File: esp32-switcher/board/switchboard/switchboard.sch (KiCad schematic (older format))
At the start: 15 parts, among them J1 Conn_01x03, J10 Conn_01x02, J11 Conn_01x02, J12 Conn_01x02, J13 Conn_01x02, J14 Conn_01x02, J2 Conn_01x04, J3 Conn_01x02, J4 Conn_01x02, J5 Conn_01x02, J6 Conn_01x02, J7 Conn_01x02, J8 Conn_01x02, J9 Conn_01x02, U1 ESP32-DEVKITC-32D

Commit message: Updates, almost ready to go
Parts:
- added J15: Chain Out, Connector_JST:JST_XH_B3B-XH-AM_1x03_P2.50mm_Vertical, symbol Connector_Generic:Conn_01x03
- J16: renamed from J1; value Conn_01x03 -> Chain In
- U1: value ESP32-DEVKITC-32D -> NODEMCU-32S
- renumbered J3 to J1, J9 to J11, J8 to J12, J2 to J17, J4 to J2, J5 to J3, J6 to J4, J7 to J5, J14 to J6, J13 to J7, J12 to J8, J11 to J9
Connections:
- net GND: now also J15.2 (Pin_2)
- net at J16.1 (Pin_1), U1.29 (IO5): now also J15.1 (Pin_1)
- net at J16.3 (Pin_3), U1.32 (IO4): now also J15.3 (Pin_3)
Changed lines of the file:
@@
 EESchema Schematic File Version 4
+LIBS:switchboard-cache
 EELAYER 29 0
 EELAYER END
@@
 $EndDescr
 $Comp
-L Connector_Generic:Conn_01x03 J1
+L Connector_Generic:Conn_01x03 J16
 U 1 1 5CA18F92
 P 6900 5150
-F 0 "J1" V 6772 5330 50  0000 L CNN
-F 1 "Conn_01x03" V 6863 5330 50  0000 L CNN
+F 0 "J16" V 6772 5330 50  0000 L CNN
+F 1 "Chain In" V 6863 5330 50  0000 L CNN
 F 2 "Connector_JST:JST_XH_B3B-XH-AM_1x03_P2.50mm_Vertical" H 6900 5150 50  0001 C CNN
 F 3 "~" H 6900 5150 50  0001 C CNN
@@
 $EndComp
 $Comp
-L Connector_Generic:Conn_01x02 J3
+L Connector_Generic:Conn_01x02 J1
 U 1 1 5CA196A9
 P 7950 2900
-F 0 "J3" H 8030 2892 50  0000 L CNN
+F 0 "J1" H 8030 2892 50  0000 L CNN
 F 1 "Conn_01x02" H 8030 2801 50  0000 L CNN
 F 2 "Connector_JST:JST_XH_B2B-XH-AM_1x02_P2.50mm_Vertical" H 7950 2900 50  0001 C CNN
@@
 $EndComp
 $Comp
-L Connector_Generic:Conn_01x04 J2
+L Connector_Generic:Conn_01x04 J17
 U 1 1 5CA19C8A
 P 6600 2250
-F 0 "J2" V 6564 1962 50  0000 R CNN
+F 0 "J17" V 6564 1962 50  0000 R CNN
 F 1 "Conn_01x04" V 6473 1962 50  0000 R CNN
 F 2 "Connector_PinSocket_2.54mm:PinSocket_1x04_P2.54mm_Vertical" H 6600 2250 50  0001 C CNN
@@
 $EndComp
 $Comp
-L Connector_Generic:Conn_01x02 J4
+L Connector_Generic:Conn_01x02 J2
 U 1 1 5CA1C04C
 P 7950 3150
-F 0 "J4" H 8030 3142 50  0000 L CNN
+F 0 "J2" H 8030 3142 50  0000 L CNN
 F 1 "Conn_01x02" H 8030 3051 50  0000 L CNN
 F 2 "Connector_JST:JST_XH_B2B-XH-AM_1x02_P2.50mm_Vertical" H 7950 3150 50  0001 C CNN
@@
 $EndComp
 $Comp
-L Connector_Generic:Conn_01x02 J5
+L Connector_Generic:Conn_01x02 J3
 U 1 1 5CA1C459
 P 7950 3400
-F 0 "J5" H 8030 3392 50  0000 L CNN
+F 0 "J3" H 8030 3392 50  0000 L CNN
 F 1 "Conn_01x02" H 8030 3301 50  0000 L CNN
 F 2 "Connector_JST:JST_XH_B2B-XH-AM_1x02_P2.50mm_Vertical" H 7950 3400 50  0001 C CNN
@@
 $EndComp
 $Comp
-L Connector_Generic:Conn_01x02 J6
+L Connector_Generic:Conn_01x02 J4
 U 1 1 5CA1E338
 P 7950 3650
-F 0 "J6" H 8030 3642 50  0000 L CNN
+F 0 "J4" H 8030 3642 50  0000 L CNN
 F 1 "Conn_01x02" H 8030 3551 50  0000 L CNN
 F 2 "Connector_JST:JST_XH_B2B-XH-AM_1x02_P2.50mm_Vertical" H 7950 3650 50  0001 C CNN
@@
 $EndComp
 $Comp
-L Connector_Generic:Conn_01x02 J7
+L Connector_Generic:Conn_01x02 J5
 U 1 1 5CA1E6C2
 P 7950 3900
-F 0 "J7" H 8030 3892 50  0000 L CNN
+F 0 "J5" H 8030 3892 50  0000 L CNN
 F 1 "Conn_01x02" H 8030 3801 50  0000 L CNN
 F 2 "Connector_JST:JST_XH_B2B-XH-AM_1x02_P2.50mm_Vertical" H 7950 3900 50  0001 C CNN
@@
 $EndComp
 $Comp
-L Connector_Generic:Conn_01x02 J8
+L Connector_Generic:Conn_01x02 J12
 U 1 1 5CA1E911
 P 3450 4500
-F 0 "J8" H 3530 4492 50  0000 L CNN
+F 0 "J12" H 3530 4492 50  0000 L CNN
 F 1 "Conn_01x02" H 3530 4401 50  0000 L CNN
 F 2 "Connector_JST:JST_XH_B2B-XH-AM_1x02_P2.50mm_Vertical" H 3450 4500 50  0001 C CNN
@@
 $EndComp
 $Comp
-L Connector_Generic:Conn_01x02 J9
+L Connector_Generic:Conn_01x02 J11
 U 1 1 5CA1EDBC
 P 3450 4250
-F 0 "J9" H 3530 4242 50  0000 L CNN
+F 0 "J11" H 3530 4242 50  0000 L CNN
 F 1 "Conn_01x02" H 3530 4151 50  0000 L CNN
 F 2 "Connector_JST:JST_XH_B2B-XH-AM_1x02_P2.50mm_Vertical" H 3450 4250 50  0001 C CNN
@@
 $EndComp
 $Comp
-L Connector_Generic:Conn_01x02 J11
+L Connector_Generic:Conn_01x02 J9
 U 1 1 5CA1F5C5
 P 3450 3750
-F 0 "J11" H 3530 3742 50  0000 L CNN
+F 0 "J9" H 3530 3742 50  0000 L CNN
 F 1 "Conn_01x02" H 3530 3651 50  0000 L CNN
 F 2 "Connector_JST:JST_XH_B2B-XH-AM_1x02_P2.50mm_Vertical" H 3450 3750 50  0001 C CNN
@@
 $EndComp
 $Comp
-L Connector_Generic:Conn_01x02 J12
+L Connector_Generic:Conn_01x02 J8
 U 1 1 5CA1F98B
 P 3450 3500
-F 0 "J12" H 3530 3492 50  0000 L CNN
+F 0 "J8" H 3530 3492 50  0000 L CNN
 F 1 "Conn_01x02" H 3530 3401 50  0000 L CNN
 F 2 "Connector_JST:JST_XH_B2B-XH-AM_1x02_P2.50mm_Vertical" H 3450 3500 50  0001 C CNN
@@
 $EndComp
 $Comp
-L Connector_Generic:Conn_01x02 J13
+L Connector_Generic:Conn_01x02 J7
 U 1 1 5CA1FBF3
 P 3450 3250
-F 0 "J13" H 3530 3242 50  0000 L CNN
+F 0 "J7" H 3530 3242 50  0000 L CNN
 F 1 "Conn_01x02" H 3530 3151 50  0000 L CNN
 F 2 "Connector_JST:JST_XH_B2B-XH-AM_1x02_P2.50mm_Vertical" H 3450 3250 50  0001 C CNN
@@
 $EndComp
 $Comp
-L Connector_Generic:Conn_01x02 J14
+L Connector_Generic:Conn_01x02 J6
 U 1 1 5CA1FEDD
 P 3450 3000
-F 0 "J14" H 3530 2992 50  0000 L CNN
+F 0 "J6" H 3530 2992 50  0000 L CNN
 F 1 "Conn_01x02" H 3530 2901 50  0000 L CNN
 F 2 "Connector_JST:JST_XH_B2B-XH-AM_1x02_P2.50mm_Vertical" H 3450 3000 50  0001 C CNN
@@
 P 5500 3700
 F 0 "U1" H 5500 4867 50  0000 C CNN
-F 1 "ESP32-DEVKITC-32D" H 5500 4776 50  0000 C CNN
+F 1 "NODEMCU-32S" H 5500 4776 50  0000 C CNN
 F 2 "MODULE_ESP32-DEVKITC-32D" H 5500 3700 50  0001 L BNN
 F 3 "" H 5500 3700 50  0001 L BNN
@@
 	6300 3600 7100 3600
 Wire Wire Line
-	6800 4000 6800 4950
-Wire Wire Line
-	7000 3700 7000 4950
+	6800 4000 6800 4550
+Wire Wire Line
+	7000 3700 7000 4650
 Text GLabel 6900 4950 1    50   Input ~ 0
 GND
@@
 Wire Wire Line
 	4350 4500 3650 4500
+$Comp
+L Connector_Generic:Conn_01x03 J15
+U 1 1 5CA1AEFD
+P 7800 5150
+F 0 "J15" V 7672 5330 50  0000 L CNN
+F 1 "Chain Out" V 7763 5330 50  0000 L CNN
+F 2 "Connector_JST:JST_XH_B3B-XH-AM_1x03_P2.50mm_Vertical" H 7800 5150 50  0001 C CNN
+F 3 "~" H 7800 5150 50  0001 C CNN
+	1    7800 5150
+	0    1    1    0
+$EndComp
+Text GLabel 7800 4950 1    50   Input ~ 0
+GND
+Wire Wire Line
+	6800 4550 7700 4550
+Wire Wire Line
+	7700 4550 7700 4950
+Connection ~ 6800 4550
+Wire Wire Line
+	6800 4550 6800 4950
+Wire Wire Line
+	7000 4650 7900 4650
+Wire Wire Line
+	7900 4650 7900 4950
+Connection ~ 7000 4650
+Wire Wire Line
+	7000 4650 7000 4950
 $EndSCHEMATC

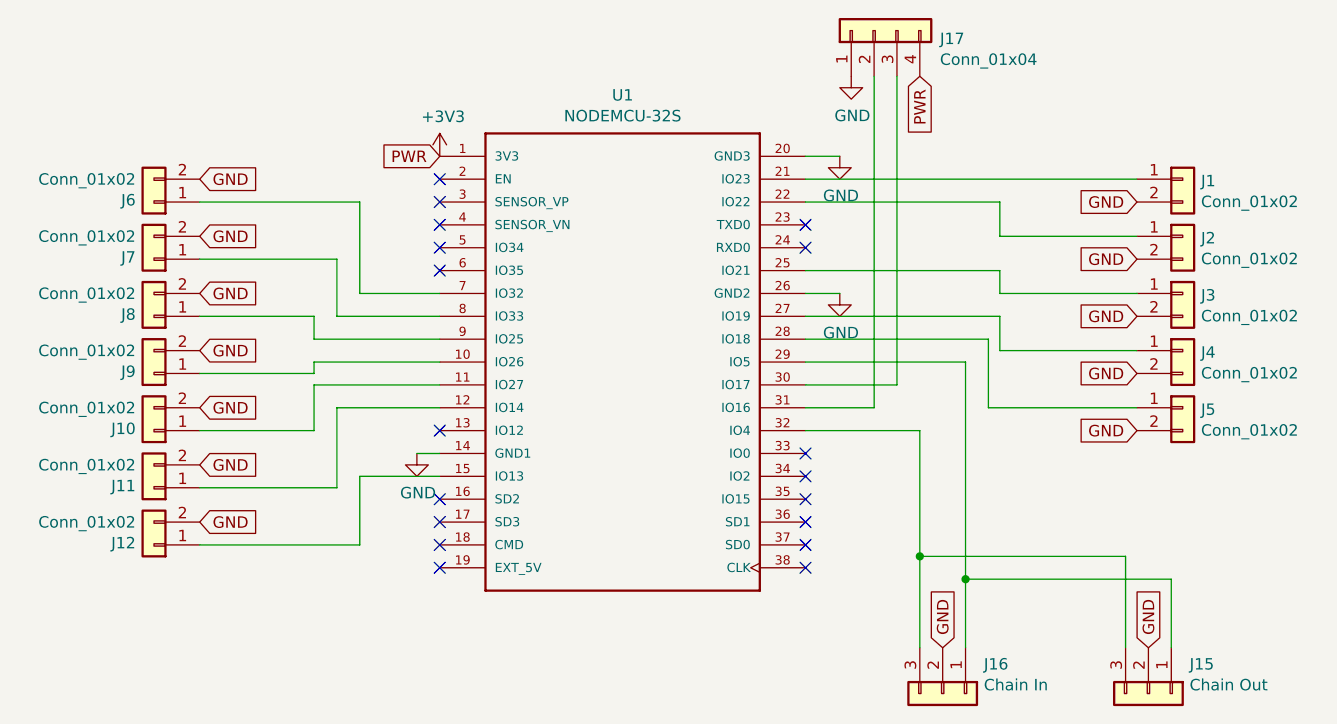
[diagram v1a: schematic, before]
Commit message: Rev 1.1 of ESP32 Switchboard
I think this rev is basically ready to go. I could see someone using
this for real. I still have a lot of software features I wanna add, but
the hardware is basically complete.

I may come back and add a built-in serial port, as the little breakout
can be flimsy, but it seems that 3v3 rs232 stuff means SMD components,
and I've been trying to avoid that to make this easier to DIY.

board:
  Converted footprint to Kicad non-legacy
  Fixed footprint to be HiLetGo ESP-E32, which is narrower than NodeMCU
  Fixed up references on schematic to be in order
  Flipped mistaken footprint on RS232 UART breakout

code:
  Added support for all 12 inputs
  IRQ-based on rising/falling edges
  Added 0.1s timer-based timeout for input switch after input off
    Fixes some bouncing in the signal I didn't expect when powering off
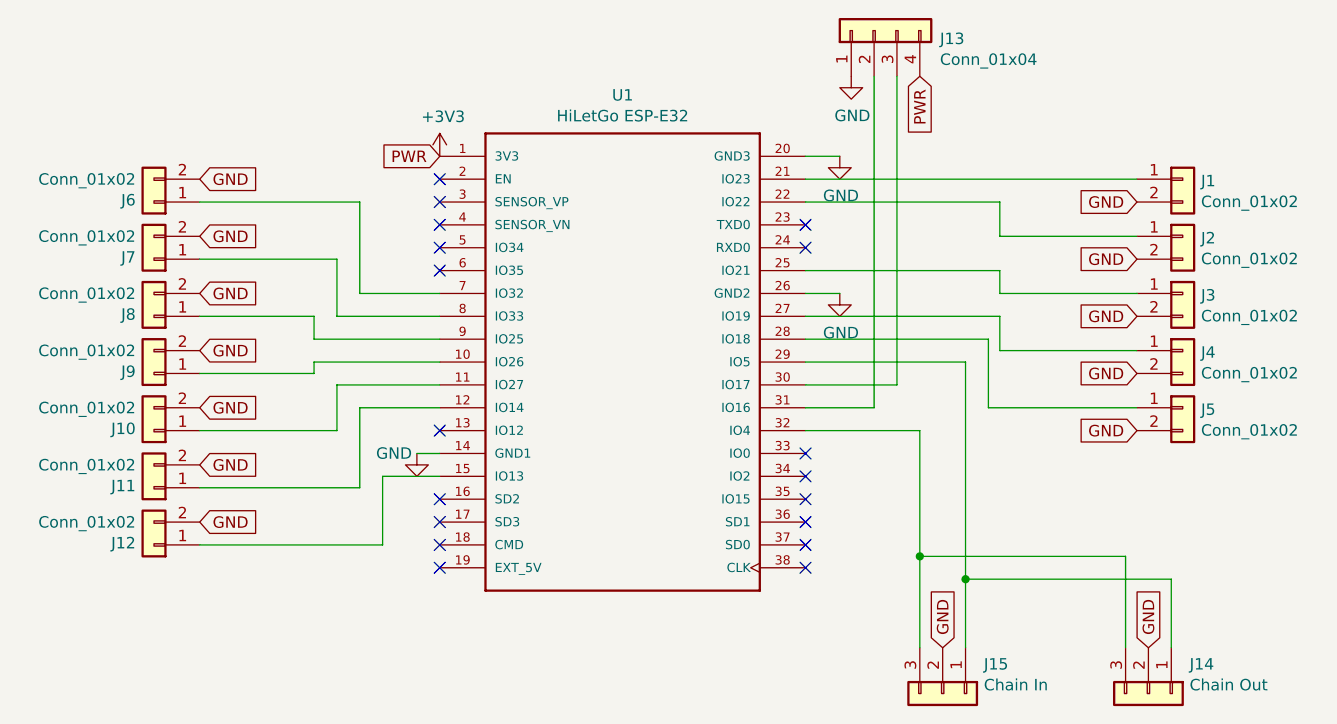
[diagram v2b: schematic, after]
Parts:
- U1: value NODEMCU-32S -> HiLetGo ESP-E32; footprint MODULE_ESP32-DEVKITC-32D -> hiletgo-e32:HILETGO-E32
- renumbered J17 to J13, J15 to J14, J16 to J15
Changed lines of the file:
@@
 encoding utf-8
 Sheet 1 1
-Title ""
-Date ""
-Rev ""
-Comp ""
-Comment1 ""
+Title "Extron ESP32 Switchboard"
+Date "2019-04-05"
+Rev "1.1"
+Comp "Rattboi (Bradon Kanyid)"
+Comment1 "https://github.com/rattboi/extron-scart-adapter"
 Comment2 ""
 Comment3 ""
@@
 $EndDescr
 $Comp
-L Connector_Generic:Conn_01x03 J16
+L Connector_Generic:Conn_01x03 J15
 U 1 1 5CA18F92
 P 6900 5150
-F 0 "J16" V 6772 5330 50  0000 L CNN
+F 0 "J15" V 6772 5330 50  0000 L CNN
 F 1 "Chain In" V 6863 5330 50  0000 L CNN
 F 2 "Connector_JST:JST_XH_B3B-XH-AM_1x03_P2.50mm_Vertical" H 6900 5150 50  0001 C CNN
@@
 $EndComp
 $Comp
-L Connector_Generic:Conn_01x04 J17
+L Connector_Generic:Conn_01x04 J13
 U 1 1 5CA19C8A
 P 6600 2250
-F 0 "J17" V 6564 1962 50  0000 R CNN
+F 0 "J13" V 6564 1962 50  0000 R CNN
 F 1 "Conn_01x04" V 6473 1962 50  0000 R CNN
 F 2 "Connector_PinSocket_2.54mm:PinSocket_1x04_P2.54mm_Vertical" H 6600 2250 50  0001 C CNN
@@
 P 4600 4100
 F 0 "#PWR0105" H 4600 3850 50  0001 C CNN
-F 1 "GND" H 4605 3927 50  0000 C CNN
+F 1 "GND" H 4500 4100 50  0000 C CNN
 F 2 "" H 4600 4100 50  0001 C CNN
 F 3 "" H 4600 4100 50  0001 C CNN
@@
 NoConn ~ 6300 4300
 Wire Wire Line
-	4700 4200 4350 4200
-Wire Wire Line
 	6300 3000 7150 3000
 Wire Wire Line
@@
 P 5500 3700
 F 0 "U1" H 5500 4867 50  0000 C CNN
-F 1 "NODEMCU-32S" H 5500 4776 50  0000 C CNN
-F 2 "MODULE_ESP32-DEVKITC-32D" H 5500 3700 50  0001 L BNN
+F 1 "HiLetGo ESP-E32" H 5500 4776 50  0000 C CNN
+F 2 "hiletgo-e32:HILETGO-E32" H 5500 3700 50  0001 L BNN
 F 3 "" H 5500 3700 50  0001 L BNN
 F 4 "Eval Board For Esp-Wroom-32" H 5500 3700 50  0001 L BNN "Field4"
@@
 	4150 3700 4700 3700
 Wire Wire Line
-	4150 3800 4150 4000
-Wire Wire Line
-	4150 4000 3650 4000
-Wire Wire Line
-	4150 3800 4700 3800
-Wire Wire Line
-	4250 3900 4250 4250
-Wire Wire Line
-	4250 4250 3650 4250
-Wire Wire Line
-	4250 3900 4700 3900
-Wire Wire Line
-	4350 4200 4350 4500
-Wire Wire Line
-	4350 4500 3650 4500
-$Comp
-L Connector_Generic:Conn_01x03 J15
+	4250 3800 4250 4000
+Wire Wire Line
+	4250 4000 3650 4000
+Wire Wire Line
+	4250 3800 4700 3800
+Wire Wire Line
+	4350 3900 4350 4250
+Wire Wire Line
+	4350 4250 3650 4250
+Wire Wire Line
+	4350 3900 4700 3900
+Wire Wire Line
+	4450 4500 3650 4500
+$Comp
+L Connector_Generic:Conn_01x03 J14
 U 1 1 5CA1AEFD
 P 7800 5150
-F 0 "J15" V 7672 5330 50  0000 L CNN
+F 0 "J14" V 7672 5330 50  0000 L CNN
 F 1 "Chain Out" V 7763 5330 50  0000 L CNN
 F 2 "Connector_JST:JST_XH_B3B-XH-AM_1x03_P2.50mm_Vertical" H 7800 5150 50  0001 C CNN
@@
 Wire Wire Line
 	7000 4650 7000 4950
+Wire Wire Line
+	4700 4200 4450 4200
+Wire Wire Line
+	4450 4200 4450 4500
 $EndSCHEMATC
